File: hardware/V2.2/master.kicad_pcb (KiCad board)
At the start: 4 copper layers, 40 x 40 mm, 125 parts, among them J101 USB-MINI-B-SMD, J102 DRILL, J103 DRILL, J104 DRILL, J105 DRILL, J301 STACK-UP-LOW, J302 STACK-DOWN, J303 STACK-UP-LOW, J304 STACK-DOWN, P201 CON-SENSOR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

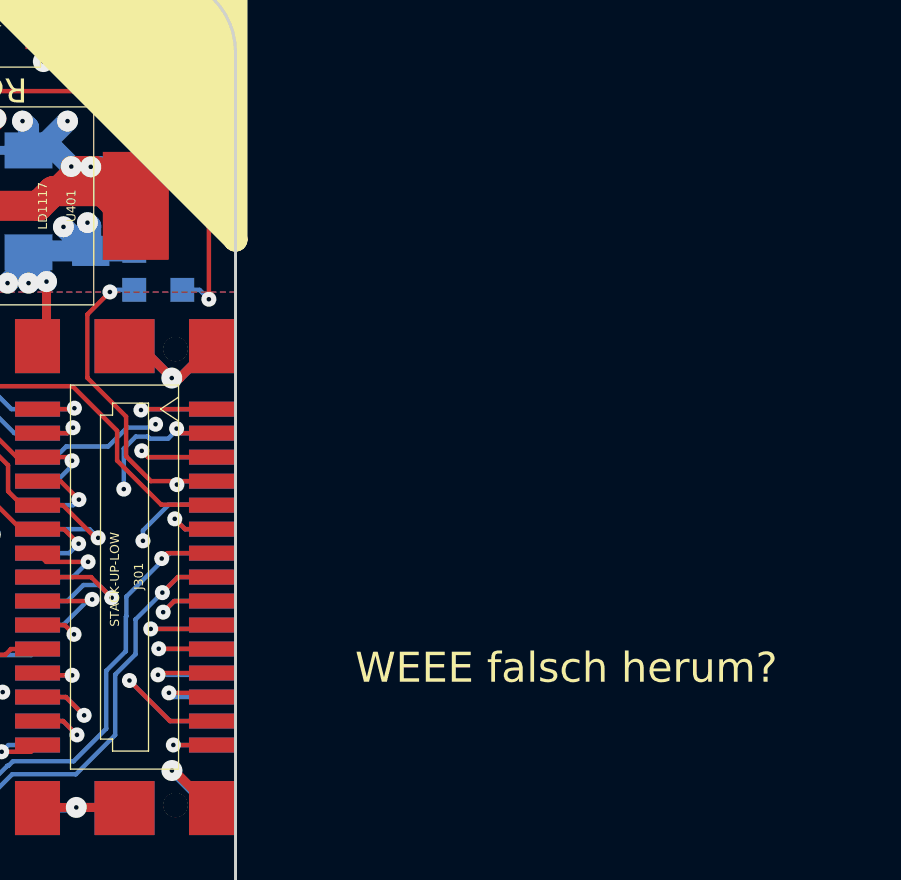
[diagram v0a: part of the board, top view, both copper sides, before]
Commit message: route vcc signal with more border clearance
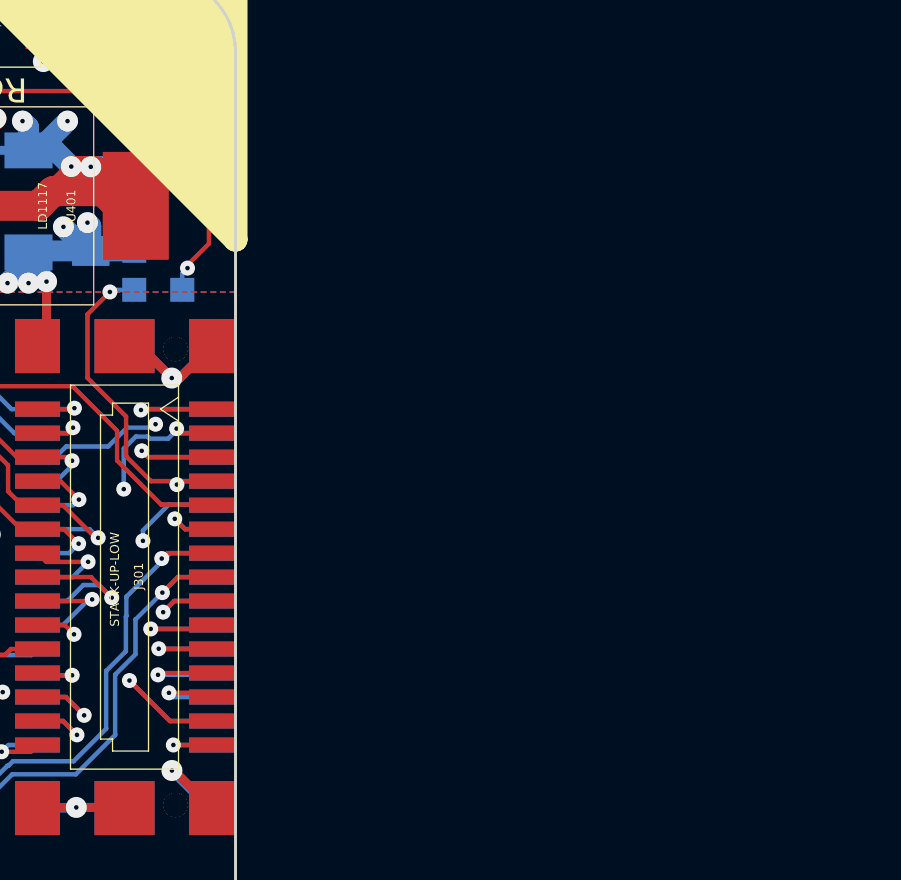
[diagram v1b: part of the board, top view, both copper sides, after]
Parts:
- removed the VAL at (156.7, 90.8)
- added VAL: WEEE_7mm_back, kicad-libraries:WEEE_7mm_back, B.Cu at (156.6, 90.8)
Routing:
- net Net-(C413-Pad1): track 119.1 -> 118.6 mm
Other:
- board text removed: "WEEE falsch herum?"

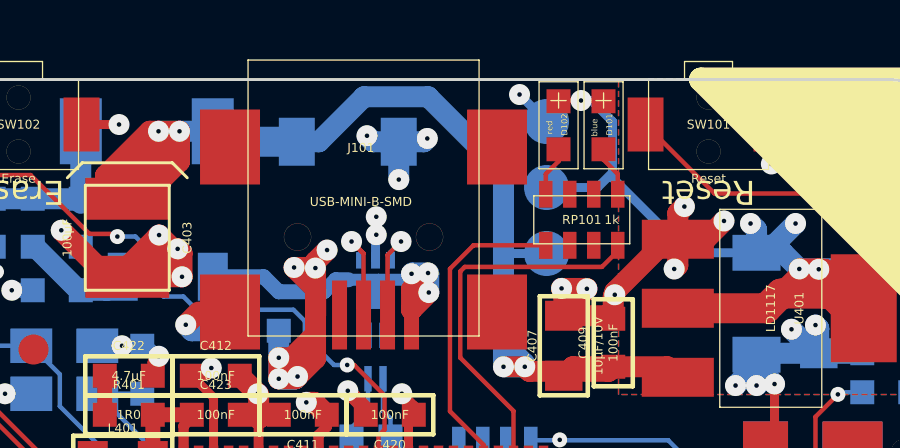
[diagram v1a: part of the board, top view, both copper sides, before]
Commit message: add more distance to border for some signals
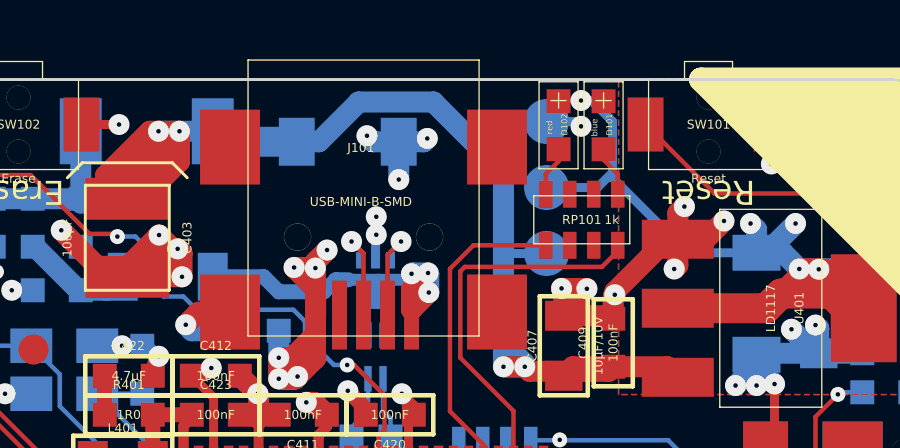
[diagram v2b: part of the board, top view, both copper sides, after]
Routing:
- net GND: track 452.2 -> 455.0 mm

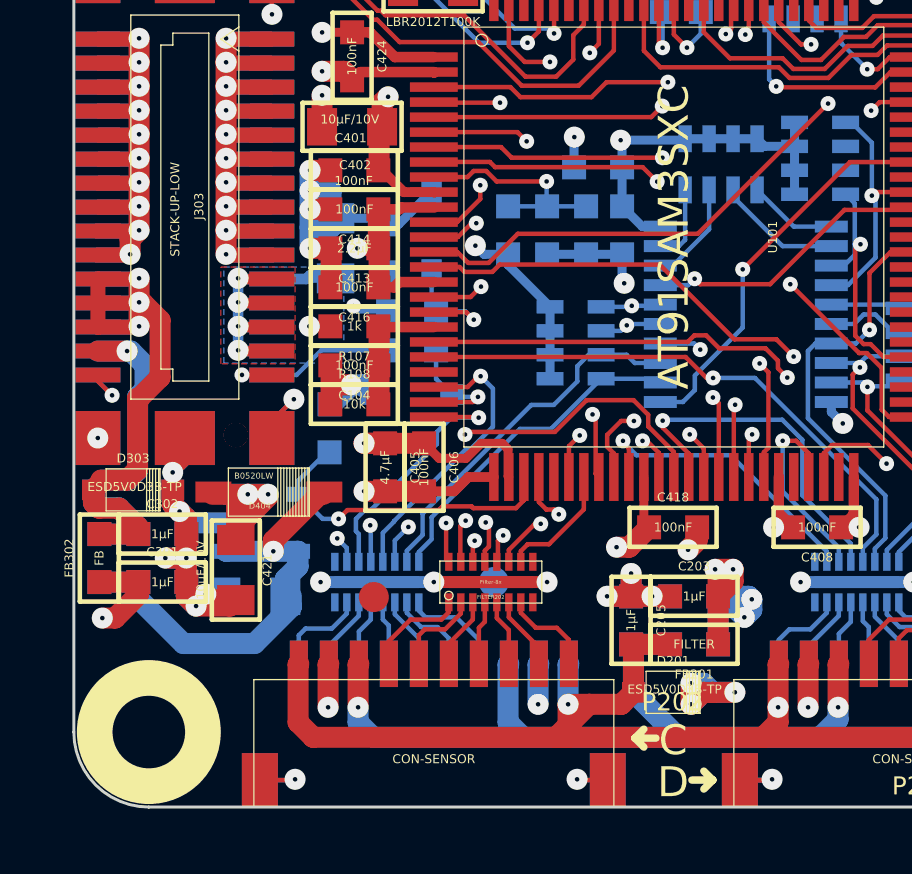
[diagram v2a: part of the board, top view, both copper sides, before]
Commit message: fix tvs diode orientation also for single tvs diode use
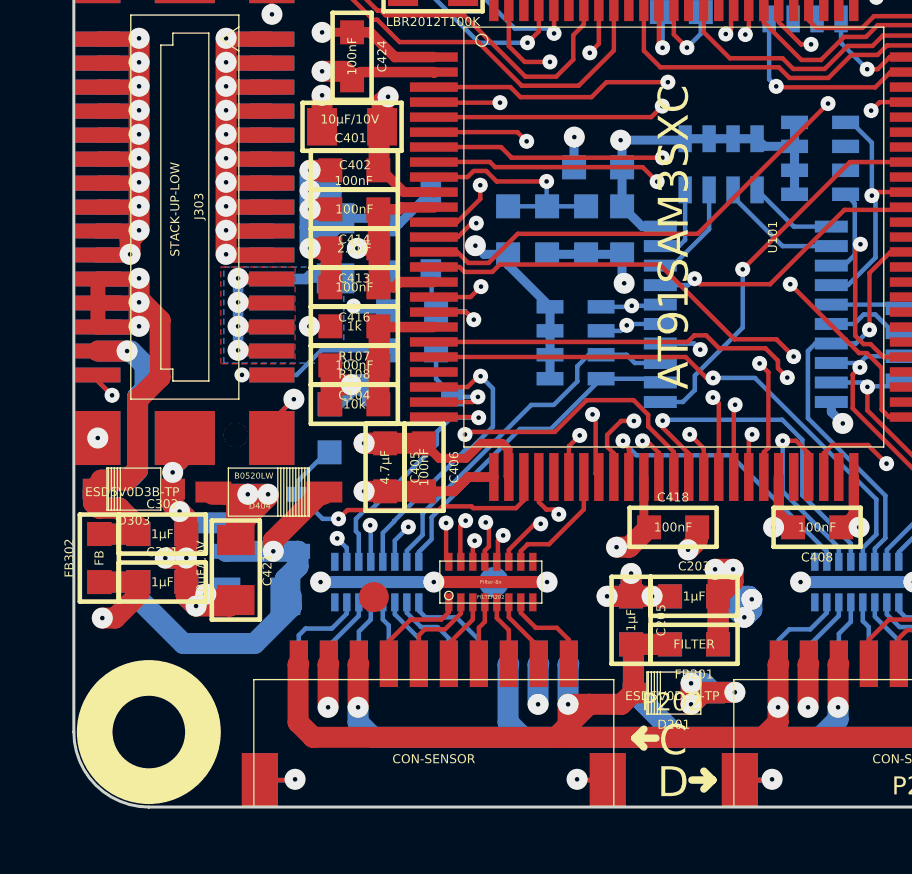
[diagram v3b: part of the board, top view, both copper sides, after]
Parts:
- moved D301 0.06 mm to (138.6, 101.2), turned to 0 degrees
- turned D201 to 180 degrees
- turned D202 to 180 degrees
- turned D303 to 180 degrees
- turned D304 to 180 degrees
- turned D302 to 270 degrees
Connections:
- D201 pad 1: Net-(C205-Pad2) -> GND
- D201 pad 2: GND -> Net-(C205-Pad2)
- D202 pad 1: Net-(C206-Pad2) -> GND
- D202 pad 2: GND -> Net-(C206-Pad2)
- D301 pad 1: STACK-CURRENT -> GND
- D301 pad 2: GND -> STACK-CURRENT
- D302 pad 1: STACK-VOLTAGE -> GND
- D302 pad 2: GND -> STACK-VOLTAGE
- D303 pad 1: Net-(C302-Pad1) -> GND
- D303 pad 2: GND -> Net-(C302-Pad1)
- D304 pad 1: Net-(C303-Pad1) -> GND
- D304 pad 2: GND -> Net-(C303-Pad1)
